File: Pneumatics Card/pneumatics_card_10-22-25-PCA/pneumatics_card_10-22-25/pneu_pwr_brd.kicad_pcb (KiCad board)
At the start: 2 copper layers, 64.2 x 63.8 mm, 63 parts, among them J2 2X1, J3 2X1, J4 2X1, J5 2X1, J6 2X1, J7 2X1, Q1 NTR0202PLT1G OR Si2347DS, Q3 FQP30N06L, Q4 FQP30N06L, Q5 FQP30N06L, Q6 FQP30N06L, Q7 IRF4905SPbF, U1 L7805, U2 LD1117V33, U3 PCA9685, U4 MCP1416, U5 TCA4307, U6 MCP1416, U7 MCP1416, U8 MCP1416

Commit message: old pneumatics
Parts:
- added BOOT_R1: 10k, Resistor_SMD:R_0805_2012Metric_Pad1.20x1.40mm_HandSolder, F.Cu at (125.6, 93.0)
- added Bulk_1: 1uF, Capacitor_SMD:C_0805_2012Metric_Pad1.18x1.45mm_HandSolder, F.Cu at (106.4, 80.9)
- added Bulk_22: 22uF, Capacitor_SMD:C_0805_2012Metric_Pad1.18x1.45mm_HandSolder, F.Cu at (93.0, 80.6)
- added Bulk_4.7: 4.7uF, Capacitor_SMD:C_0805_2012Metric_Pad1.18x1.45mm_HandSolder, F.Cu at (106.4, 83.2)
- added C10: 10pF, Capacitor_SMD:C_0402_1005Metric_Pad0.74x0.62mm_HandSolder, F.Cu at (104.7, 90.4)
- added C11: 10pF, Capacitor_SMD:C_0402_1005Metric_Pad0.74x0.62mm_HandSolder, F.Cu at (107.5, 93.2)
- added C12: 0.47u, Capacitor_SMD:C_0402_1005Metric, F.Cu at (84.5, 100.5)
- added C13: 1uF, Capacitor_SMD:C_0402_1005Metric, F.Cu at (126.3, 68.3)
- added C14: 0.1uF, Capacitor_SMD:C_0402_1005Metric, F.Cu at (127.3, 68.3)
- added C15: 0.1uF, Capacitor_SMD:C_0402_1005Metric, F.Cu at (85.5, 67.8)
- added C16: 1uF, Capacitor_SMD:C_0402_1005Metric, F.Cu at (86.5, 67.8)
- added C16: 0.1u, Capacitor_SMD:C_0603_1608Metric, F.Cu at (108.0, 102.0)
- added C17: 0.1uF, Capacitor_SMD:C_0402_1005Metric, F.Cu at (112.4, 68.5)
- added C18: 1uF, Capacitor_SMD:C_0402_1005Metric, F.Cu at (113.5, 68.5)
- added C19: 0.1uF, Capacitor_SMD:C_0402_1005Metric, F.Cu at (99.0, 68.2)
- added C2: 10u, Capacitor_THT:CP_Radial_D5.0mm_P2.00mm, F.Cu at (83.0, 91.0)
- added C20: 1uF, Capacitor_SMD:C_0402_1005Metric, F.Cu at (100.1, 68.2)
- added C25: 0.1u, Capacitor_SMD:C_0603_1608Metric, F.Cu at (109.6, 96.1)
- added C3: 10u, Capacitor_THT:CP_Radial_D5.0mm_P2.00mm, F.Cu at (82.9, 85.3)
- added C4: 10u, Capacitor_THT:CP_Radial_D5.0mm_P2.00mm, F.Cu at (100.2, 88.5)
- added C5: 22nF, Capacitor_SMD:C_0402_1005Metric, F.Cu at (86.9, 103.8)
- added C7: 100nF, Capacitor_SMD:C_0805_2012Metric_Pad1.18x1.45mm_HandSolder, F.Cu at (105.3, 86.5)
- added C8: 100nF, Capacitor_SMD:C_0805_2012Metric_Pad1.18x1.45mm_HandSolder, F.Cu at (107.4, 86.5)
- added C9: 100nF, Capacitor_SMD:C_0805_2012Metric_Pad1.18x1.45mm_HandSolder, B.Cu at (113.0, 85.5)
- added D1: 1N47xxA, Diode_THT:D_DO-41_SOD81_P10.16mm_Horizontal, F.Cu at (120.6, 59.4)
- added D2: 1N47xxA, Diode_THT:D_DO-41_SOD81_P10.16mm_Horizontal, F.Cu at (107.1, 59.5)
- added D3: 1N47xxA, Diode_THT:D_DO-41_SOD81_P10.16mm_Horizontal, F.Cu at (93.6, 59.8)
- added D4: 1N47xxA, Diode_THT:D_DO-41_SOD81_P10.16mm_Horizontal, F.Cu at (80.3, 59.5)
- added F1: 10A, Fuse:Fuse_1206_3216Metric, F.Cu at (91.5, 101.0)
- added H1: MountingHole, MountingHole:MountingHole_3.2mm_M3_DIN965, F.Cu at (79.0, 48.5)
- added H2: MountingHole, MountingHole:MountingHole_3.2mm_M3_DIN965, F.Cu at (132.0, 48.5)
- added H3: MountingHole, MountingHole:MountingHole_3.2mm_M3_DIN965, F.Cu at (79.0, 103.5)
- added H4: MountingHole, MountingHole:MountingHole_3.2mm_M3_DIN965, F.Cu at (132.0, 103.5)
- added J1: 2X1, Connector_JST:JST_PH_B2B-PH-K_1x02_P2.00mm_Vertical, F.Cu at (110.7, 105.0)
- added J10: Conn_01x02, Connector_PinHeader_2.54mm:PinHeader_1x02_P2.54mm_Vertical, F.Cu at (82.3, 78.7)
- added J11: Conn_01x02, Connector_PinHeader_2.54mm:PinHeader_1x02_P2.54mm_Vertical, F.Cu at (82.3, 74.9)
- added J12: 2X1, Connector_JST:JST_PH_B2B-PH-K_1x02_P2.00mm_Vertical, F.Cu at (77.8, 74.6)
- added J2: 2X1, Connector_JST:JST_PH_B2B-PH-K_1x02_P2.00mm_Vertical, F.Cu at (92.8, 104.8)
- added J3: 2X1, Connector_JST:JST_PH_B2B-PH-K_1x02_P2.00mm_Vertical, F.Cu at (127.5, 61.4)
- added J4: 2X1, Connector_JST:JST_PH_B2B-PH-K_1x02_P2.00mm_Vertical, F.Cu at (114.0, 61.7)
- added J5: 2X1, Connector_JST:JST_PH_B2B-PH-K_1x02_P2.00mm_Vertical, F.Cu at (100.4, 61.4)
- added J6: 2X1, Connector_JST:JST_PH_B2B-PH-K_1x02_P2.00mm_Vertical, F.Cu at (86.9, 60.7)
- added J7: Conn_01x03_Pin, Connector_PinHeader_2.54mm:PinHeader_1x03_P2.54mm_Vertical, F.Cu at (127.6, 96.3)
- added J8: Conn_01x03, custom_components:slide_switch_EGER1218_Thruster, F.Cu at (125.7, 83.4)
- added J9: Conn_01x03_Pin, Connector_PinHeader_2.54mm:PinHeader_1x03_P2.54mm_Vertical, F.Cu at (130.1, 81.7)
- added Q1: NTR0202PLT1G OR Si2347DS, Package_TO_SOT_SMD:SOT-23-3, F.Cu at (87.1, 101.0)
- added Q3: FQP30N06L, Package_TO_SOT_THT:TO-220-3_Vertical, F.Cu at (126.7, 54.5)
- added Q4: FQP30N06L, Package_TO_SOT_THT:TO-220-3_Vertical, F.Cu at (113.2, 54.5)
- added Q5: FQP30N06L, Package_TO_SOT_THT:TO-220-3_Vertical, F.Cu at (99.8, 54.8)
- added Q6: FQP30N06L, Package_TO_SOT_THT:TO-220-3_Vertical, F.Cu at (86.4, 54.5)
- added R1: 1k, Resistor_SMD:R_0402_1005Metric, F.Cu at (88.1, 103.8)
- added R10: 330, Resistor_SMD:R_0805_2012Metric_Pad1.20x1.40mm_HandSolder, F.Cu at (90.3, 63.5)
- added R11: 10k, Resistor_SMD:R_0805_2012Metric_Pad1.20x1.40mm_HandSolder, F.Cu at (85.4, 52.0)
- added R12: 10k, Resistor_SMD:R_0603_1608Metric, F.Cu at (106.5, 99.9)
- added R14: 10k, Resistor_SMD:R_0603_1608Metric, F.Cu at (116.2, 99.7)
- added R15: 10k, Resistor_SMD:R_0603_1608Metric, F.Cu at (106.5, 96.8)
- added R16: 10k, Resistor_SMD:R_0603_1608Metric, F.Cu at (106.5, 98.3)
- added R17: 10k, Resistor_SMD:R_0603_1608Metric, F.Cu at (116.2, 98.2)
- added R18: 10k, Resistor_SMD:R_0603_1608Metric, F.Cu at (116.2, 101.3)
- added R2: 4.7k, Resistor_SMD:R_0402_1005Metric, F.Cu at (85.5, 103.8)
- added R4: 330, Resistor_SMD:R_0805_2012Metric_Pad1.20x1.40mm_HandSolder, F.Cu at (131.0, 64.0)
- added R5: 10k, Resistor_SMD:R_0805_2012Metric_Pad1.20x1.40mm_HandSolder, F.Cu at (125.7, 51.9)
- added R6: 330, Resistor_SMD:R_0805_2012Metric_Pad1.20x1.40mm_HandSolder, F.Cu at (117.2, 64.4)
- added R7: 10k, Resistor_SMD:R_0805_2012Metric_Pad1.20x1.40mm_HandSolder, F.Cu at (112.2, 52.0)
- added R8: 330, Resistor_SMD:R_0805_2012Metric_Pad1.20x1.40mm_HandSolder, F.Cu at (103.7, 64.0)
- added R9: 10k, Resistor_SMD:R_0805_2012Metric_Pad1.20x1.40mm_HandSolder, F.Cu at (99.1, 52.2)
- added T_Cd1: 100nF, Capacitor_SMD:C_0805_2012Metric_Pad1.18x1.45mm_HandSolder, F.Cu at (95.8, 76.7)
- added T_Cd2: 100nF, Capacitor_SMD:C_0805_2012Metric_Pad1.18x1.45mm_HandSolder, F.Cu at (89.1, 80.5)
- added U1: L7805, Package_TO_SOT_THT:TO-220-3_Vertical, F.Cu at (78.5, 91.3)
- added U2: LD1117V33, Package_TO_SOT_THT:TO-220-3_Vertical, F.Cu at (95.8, 91.3)
- added U3: MCP1416, Package_TO_SOT_SMD:SOT-23-5, F.Cu at (129.9, 67.8)
- added U4: MCP1416, Package_TO_SOT_SMD:SOT-23-5, F.Cu at (116.1, 68.0)
- added U5: TCA4307, custom_components:SOIC8_DGK_TEX, F.Cu at (111.3, 99.0)
- added U8: MCP1416, Package_TO_SOT_SMD:SOT-23-5, F.Cu at (102.7, 67.8)
- added U9: MCP1416, Package_TO_SOT_SMD:SOT-23-5, F.Cu at (89.1, 67.2)
- added Y1: 16Mhz, Crystal:Crystal_SMD_3225-4Pin_3.2x2.5mm, F.Cu at (105.2, 93.0)
- renumbered U3 to U10
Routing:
- net 3.3V: track 0.00 -> 94.4 mm, vias 0 -> 2
- net GND: track 46.2 -> 100.3 mm, vias 1 -> 60
- net S4CTRL: track 37.1 -> 68.9 mm
- net 5V: track 0.00 -> 23.3 mm, vias 0 -> 2
- net FDCAN_RX: track 0.00 -> 22.8 mm
- net FDCAN_TX: track 0.00 -> 20.4 mm
- net S3CTRL: track 20.8 -> 39.9 mm
- net S1CTRL: track 4.91 -> 22.4 mm
- net 12V: track 1.49 -> 18.9 mm, vias 16 -> 36
- net /NRST: track 0.00 -> 16.6 mm
- net USART+: track 0.00 -> 14.9 mm
- net /SWCLK: track 0.00 -> 14.7 mm
- net S2CTRL: track 7.99 -> 21.7 mm
- net USART-: track 0.00 -> 13.3 mm
- net /SWDIO: track 0.00 -> 13.1 mm
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- added copper zone on F.Cu, net GND
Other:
- board size 64.2 x 63.8 mm -> 131.7 x 65.2 mm
- board text added: "12V to 3.3V"
- board text added: "12V to 5V"
- board text added: "3.3V GND GND"
- board text added: "ATA6561"
- board text added: "CAN+"
- board text added: "CAN-"
- board text added: "CAN- CAN+"
- board text added: "NRST SWDIO SWCLK"
- board text added: "SCL"
- board text added: "SDA"
- board text added: "USART_RX"
- board text added: "USART_TX"

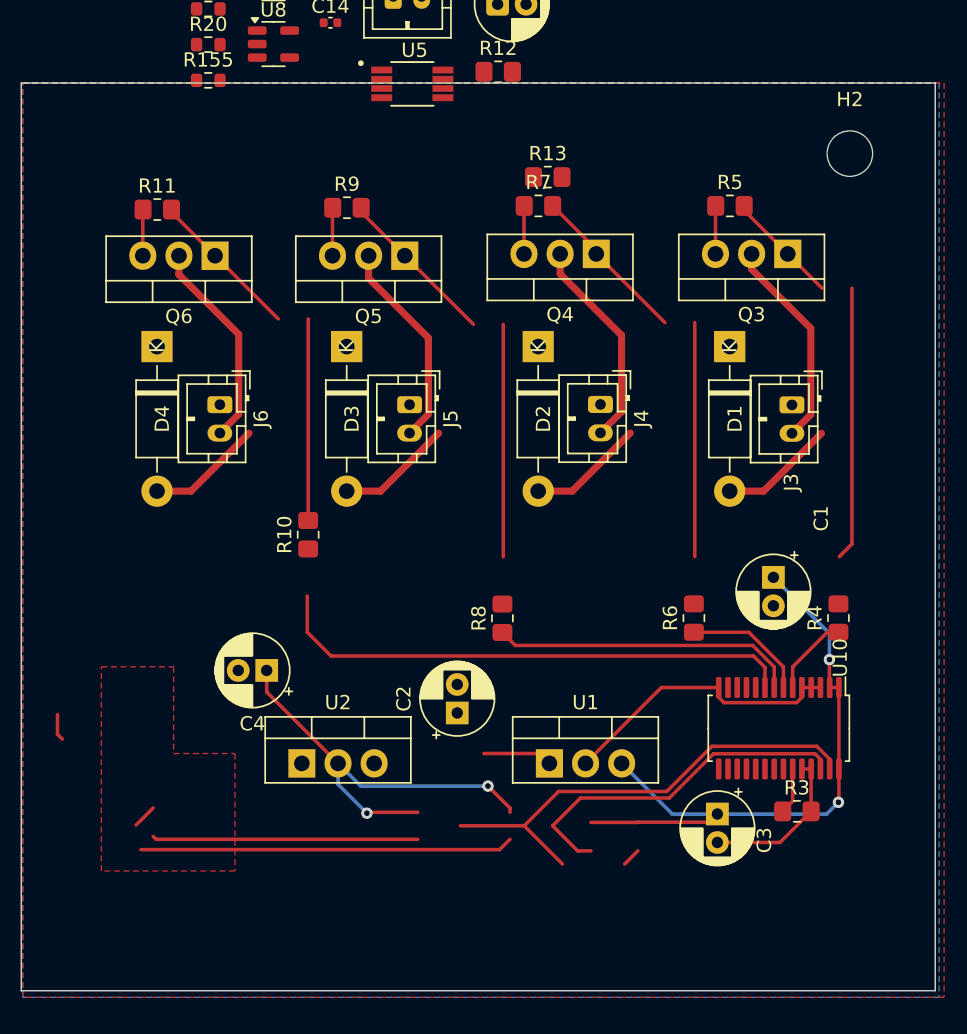
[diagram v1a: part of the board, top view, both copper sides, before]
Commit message: old pneumatics added mounting holes
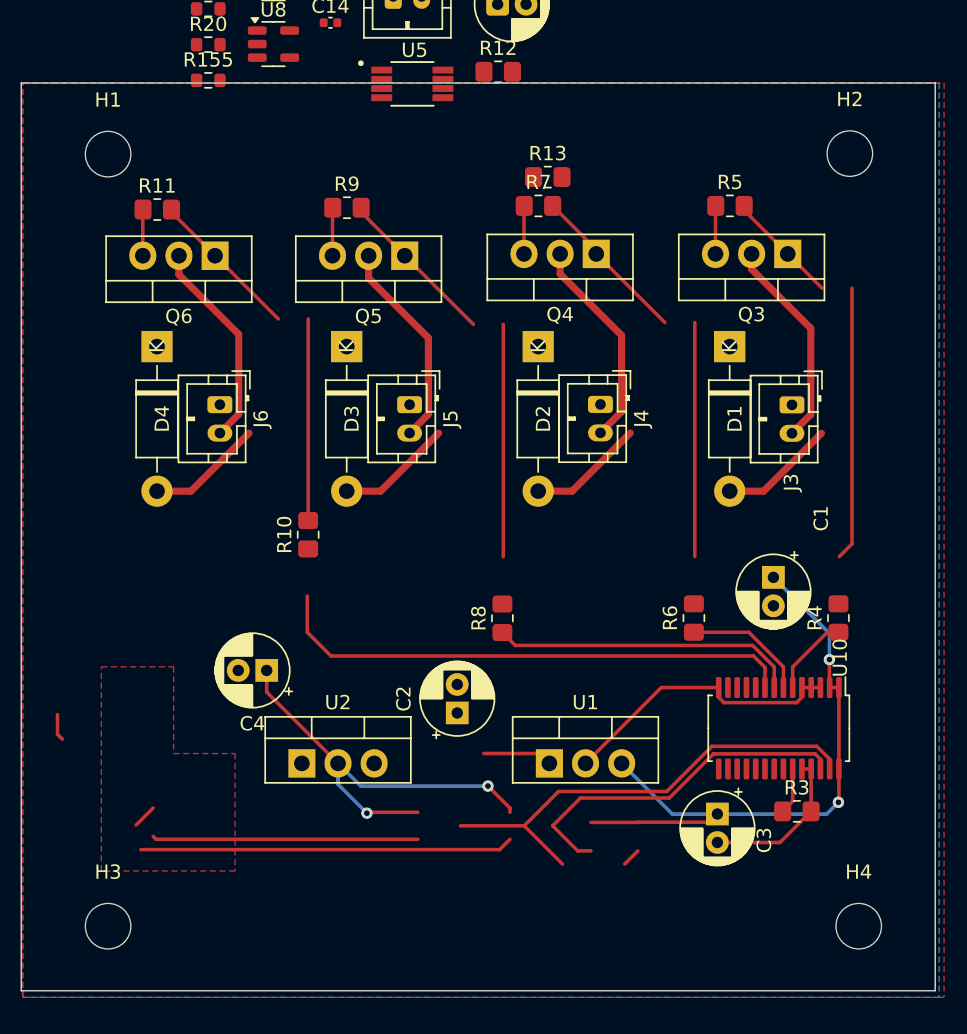
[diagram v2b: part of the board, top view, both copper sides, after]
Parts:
- added H1: MountingHole, MountingHole:MountingHole_3.2mm_M3_DIN965, F.Cu at (146.5, 48.3)
- added H3: MountingHole, MountingHole:MountingHole_3.2mm_M3_DIN965, F.Cu at (146.5, 102.6)
- added H4: MountingHole, MountingHole:MountingHole_3.2mm_M3_DIN965, F.Cu at (199.2, 102.6)

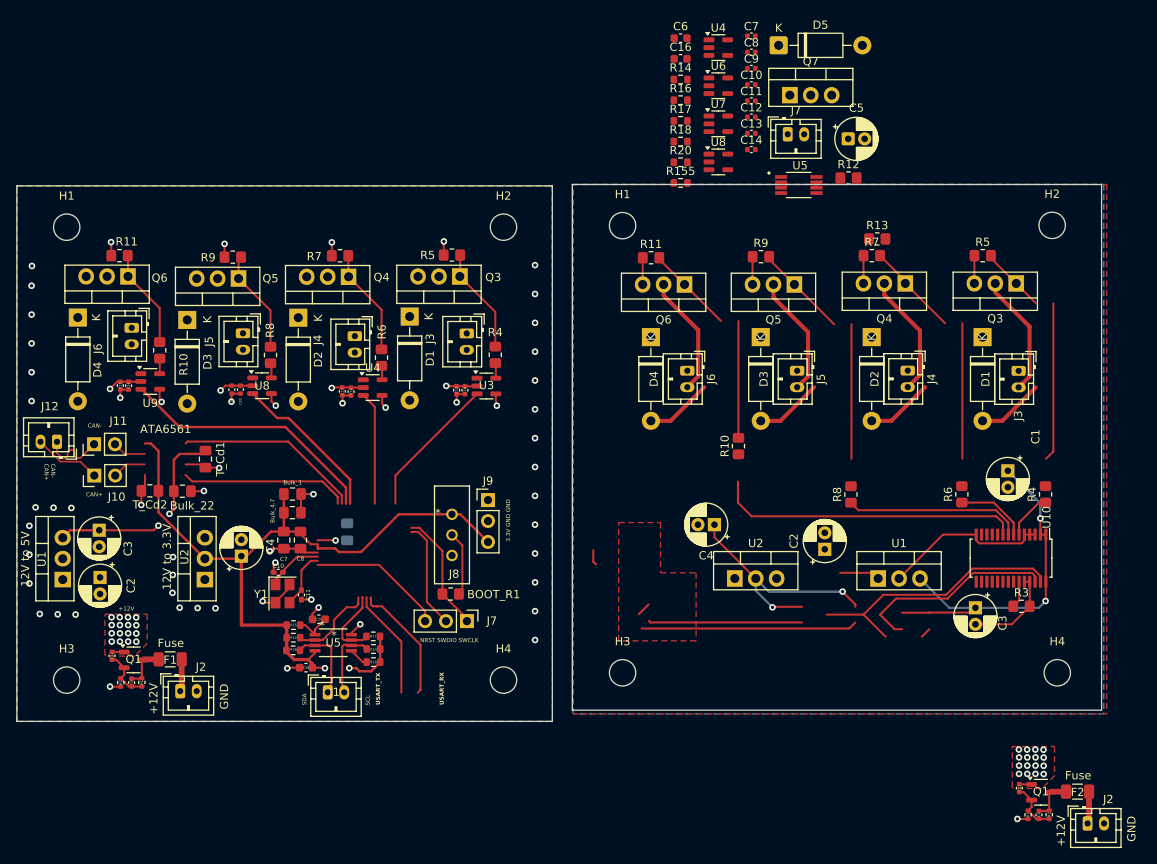
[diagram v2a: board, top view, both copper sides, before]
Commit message: routed pneumatics pcb
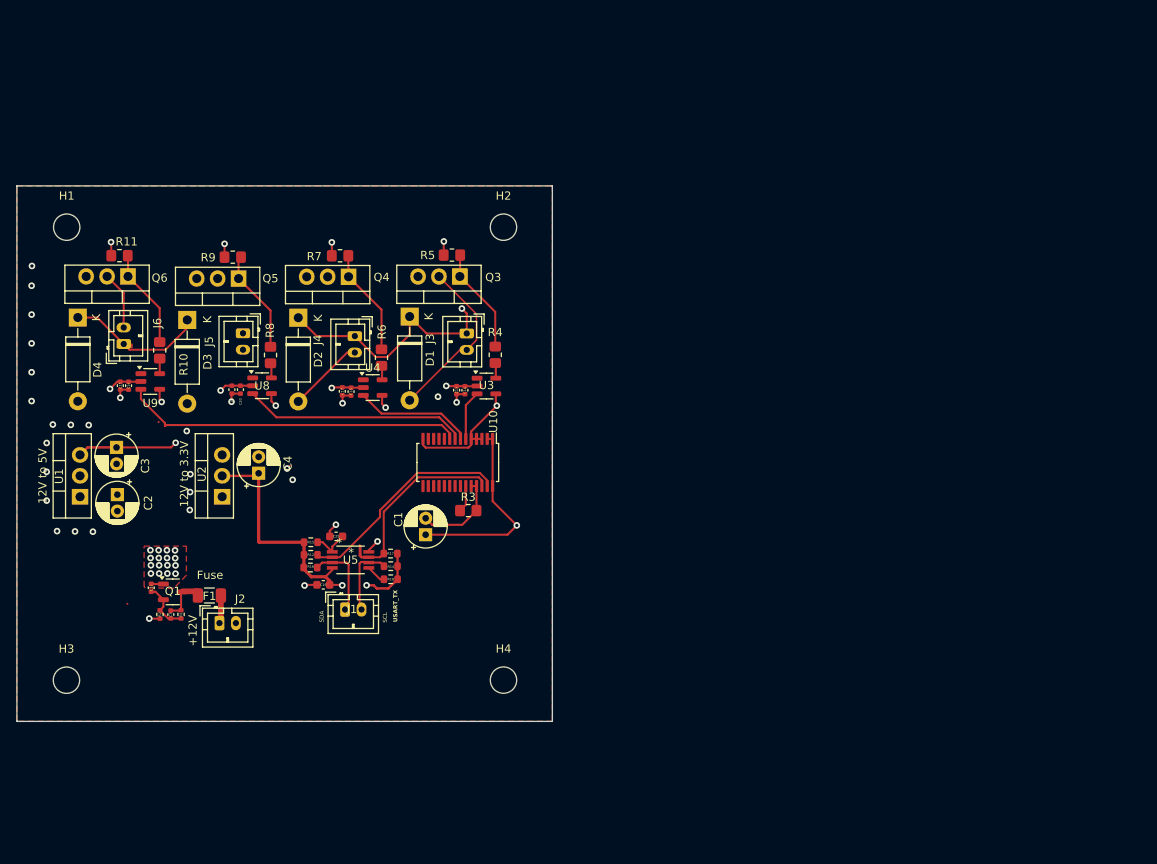
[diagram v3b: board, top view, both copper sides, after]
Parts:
- removed BOOT_R1: 10k, Resistor_SMD:R_0805_2012Metric_Pad1.20x1.40mm_HandSolder
- removed Bulk_1: 1uF, Capacitor_SMD:C_0805_2012Metric_Pad1.18x1.45mm_HandSolder
- removed Bulk_22: 22uF, Capacitor_SMD:C_0805_2012Metric_Pad1.18x1.45mm_HandSolder
- removed Bulk_4.7: 4.7uF, Capacitor_SMD:C_0805_2012Metric_Pad1.18x1.45mm_HandSolder
- removed C10, C11: 10pF, Capacitor_SMD:C_0402_1005Metric_Pad0.74x0.62mm_HandSolder
- removed C10, C8: 1uF, Capacitor_SMD:C_0402_1005Metric
- removed C11, C7, C9: 0.1uF, Capacitor_SMD:C_0402_1005Metric
- removed the C12 at (84.5, 100.5)
- removed the C12 at (162.1, 35.2)
- removed the C13 at (162.1, 37.1)
- removed the C14 at (162.1, 39.1)
- removed the C16 at (153.5, 28.1)
- removed the C2 at (171.0, 87.6)
- removed the C3 at (189.3, 94.7)
- removed the C4 at (157.6, 84.6)
- removed the C5 at (173.8, 37.8)
- removed the C5 at (86.9, 103.8)
- removed C6: 0.1u, Capacitor_SMD:C_0603_1608Metric
- removed C7, C8, C9, T_Cd1, T_Cd2: 100nF, Capacitor_SMD:C_0805_2012Metric_Pad1.18x1.45mm_HandSolder
- removed the D1 at (190.2, 61.9)
- removed the D2 at (176.7, 61.9)
- removed the D3 at (163.2, 61.9)
- removed the D4 at (149.9, 61.9)
- removed D5: 1N47xxA, Diode_THT:D_DO-41_SOD81_P10.16mm_Horizontal
- removed the F1 at (91.5, 101.0)
- removed the H1 at (146.5, 48.3)
- removed the H2 at (198.6, 48.3)
- removed the H3 at (146.5, 102.6)
- removed the H4 at (199.2, 102.6)
- removed J10, J11: Conn_01x02, Connector_PinHeader_2.54mm:PinHeader_1x02_P2.54mm_Vertical
- removed J12, J7: 2X1, Connector_JST:JST_PH_B2B-PH-K_1x02_P2.00mm_Vertical
- removed the J2 at (92.8, 104.8)
- removed the J3 at (194.5, 66.0)
- removed the J4 at (181.1, 65.9)
- removed the J5 at (167.6, 65.9)
- removed the J6 at (154.3, 65.9)
- removed J7, J9: Conn_01x03_Pin, Connector_PinHeader_2.54mm:PinHeader_1x03_P2.54mm_Vertical
- removed J8: Conn_01x03, custom_components:slide_switch_EGER1218_Thruster
- removed the Q1 at (87.1, 101.0)
- removed the Q3 at (194.2, 55.4)
- removed the Q4 at (180.8, 55.4)
- removed the Q5 at (167.3, 55.5)
- removed the Q6 at (154.0, 55.5)
- removed Q7: IRF4905SPbF, Package_TO_SOT_THT:TO-220-3_Vertical
- removed the R1 at (88.1, 103.8)
- removed the R10 at (160.5, 75.1)
- removed the R11 at (149.9, 52.2)
- removed the R12 at (173.9, 42.5)
- removed R13: 100k, Resistor_SMD:R_0805_2012Metric_Pad1.20x1.40mm_HandSolder
- removed the R14 at (153.5, 30.6)
- removed R155, R20: 10k, Resistor_SMD:R_0603_1608Metric
- removed the R16 at (153.5, 33.1)
- removed the R17 at (153.5, 35.6)
- removed the R18 at (153.5, 38.1)
- removed the R2 at (85.5, 103.8)
- removed the R4 at (197.8, 81.0)
- removed the R5 at (190.2, 52.0)
- removed the R6 at (187.6, 81.0)
- removed the R7 at (176.7, 52.0)
- removed the R8 at (174.2, 81.0)
- removed the R9 at (163.2, 52.1)
- removed the U1 at (177.5, 91.2)
- removed the U2 at (160.1, 91.2)
- removed the U4 at (158.1, 26.7)
- removed the U5 at (167.8, 43.4)
- removed U6, U7: MCP1416, Package_TO_SOT_SMD:SOT-23-5
- removed the U8 at (158.1, 40.6)
- removed Y1: 16Mhz, Crystal:Crystal_SMD_3225-4Pin_3.2x2.5mm
- moved C12 108.1 mm to (89.2, 92.3)
- moved J2 108.1 mm to (97.5, 96.6)
- moved R1 108.1 mm to (92.9, 95.5)
- moved R2 108.1 mm to (90.3, 95.5)
- moved C5 108.1 mm to (91.6, 95.5)
- moved Q1 108.1 mm to (91.9, 92.8)
- moved F1 108.0 mm to (96.3, 93.2)
- moved C1 71.1 mm to (122.5, 85.8), turned to 90 degrees
- moved R3 68.2 mm to (127.7, 82.9)
- moved U10 68.2 mm to (126.5, 77.1)
- moved U5 10.3 mm to (113.4, 88.9)
- moved C2 10.3 mm to (85.1, 81.0)
- moved C3 10.3 mm to (85.0, 75.3)
- moved C4 10.3 mm to (102.3, 78.4)
- moved R12 10.3 mm to (108.6, 89.8)
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- renumbered C1 to C5, F2 to F1
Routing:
- net 3.3V: track 94.4 -> 37.1 mm
- net GND: track 100.3 -> 53.3 mm, vias 60 -> 37
- net 12V: track 18.9 -> 64.6 mm, vias 36 -> 21
- net SDA: track 71.1 -> 25.8 mm
- net +3.3V: track 30.6 -> 0.00 mm, vias 2 -> 0
- net Net-(Q4-G): track 41.0 -> 13.0 mm
- net Net-(Q5-G): track 40.4 -> 12.6 mm
- net S4CTRL: track 68.9 -> 41.4 mm
- net Net-(Q3-G): track 40.2 -> 12.9 mm
- net Net-(Q6-G): track 37.1 -> 12.1 mm
- net SLN3-: track 23.0 -> 0.00 mm
- net FDCAN_RX: track 22.8 -> 0.00 mm
- net (no net): track 22.3 -> 0.00 mm
- net FDCAN_TX: track 20.4 -> 0.00 mm
- net +5V: track 44.3 -> 24.0 mm, vias 2 -> 1
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- removed copper zone on B.Cu, net GND
- removed copper zone on F.Cu, net Net-(J2-Pin_1)
- removed copper zone on F.Cu, net SLN1+
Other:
- board size 131.7 x 65.2 mm -> 65 x 65 mm
- board text removed: "3.3V GND GND"
- board text removed: "ATA6561"
- board text removed: "CAN+"
- board text removed: "CAN-"
- board text removed: "CAN- CAN+"
- board text removed: "GND"
- board text removed: "NRST SWDIO SWCLK"
- board text removed: "USART_RX"
